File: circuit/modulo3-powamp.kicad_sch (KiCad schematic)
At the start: 60 parts, among them J1 HOLE, J2 HOLE, J3 HOLE, J4 HOLE, J5 CONN_01X04, Q1 BS170, SW1 reset, SW3 HEAD/AD, U2 TPA3220, U5 PWR_CONN, U6 AMPCTRL

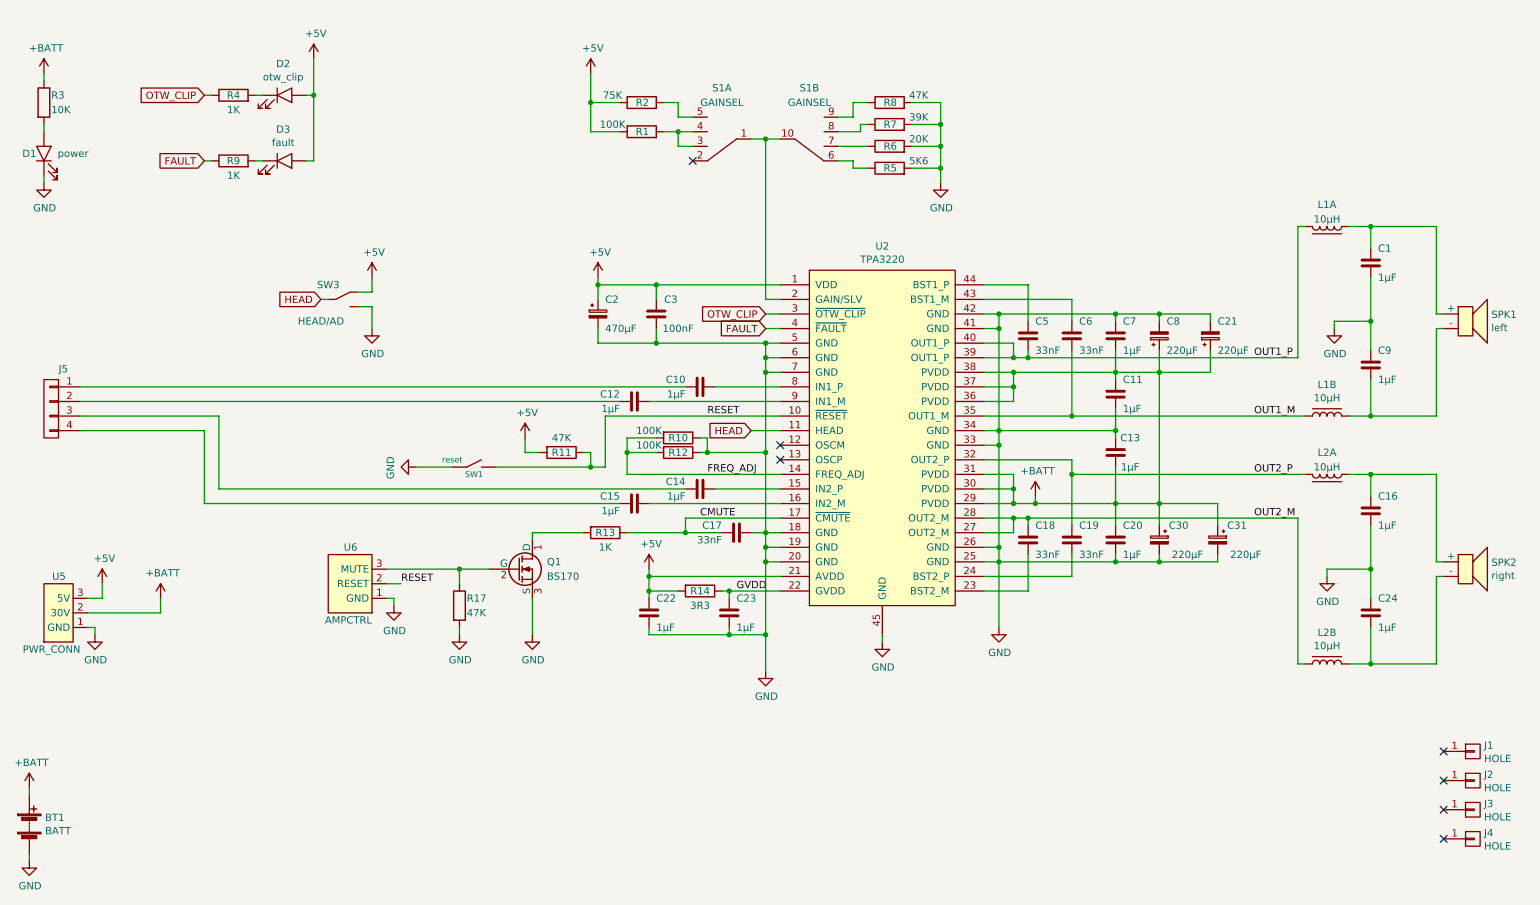
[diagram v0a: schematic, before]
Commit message: added ampctrl and diffaudio; started changing powamp
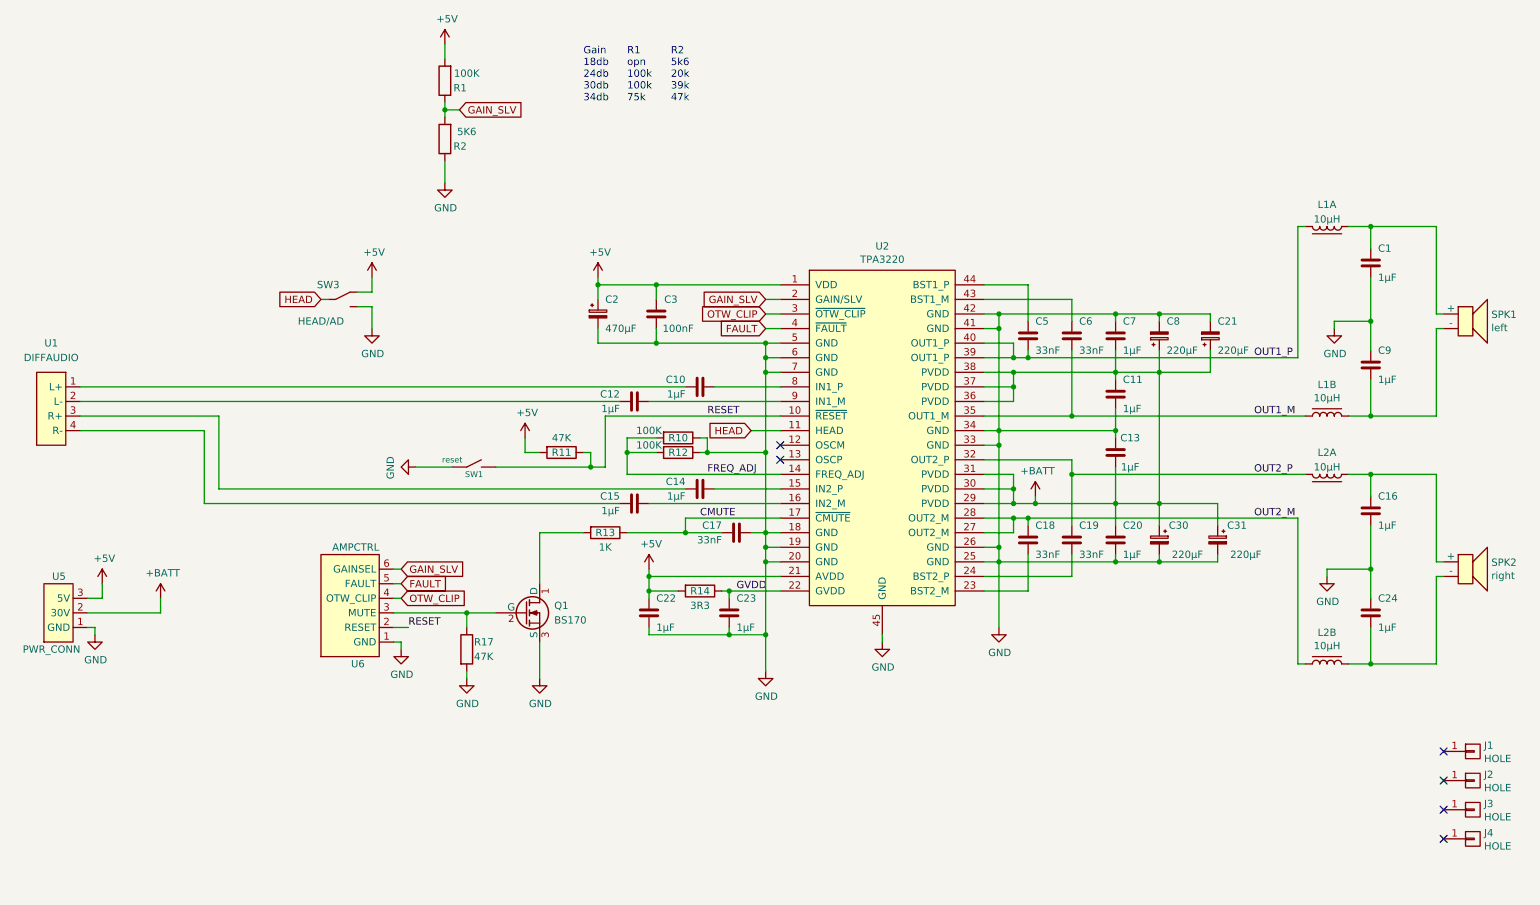
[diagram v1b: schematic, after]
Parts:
- removed BT1: BATT, myAmp:BATTERY, symbol myAmp:Battery
- removed D1: power, myAmp:LED_D3.0mm_PCBedge, symbol myAmp:LED
- removed D2: otw_clip, myAmp:LED_D3.0mm_PCBedge, symbol myAmp:LED
- removed D3: fault, myAmp:LED_D3.0mm_PCBedge, symbol myAmp:LED
- removed J5: CONN_01X04, myAmp:PIN_1x04, symbol myAmp:CONN_01X04
- removed R3: 10K, myAmp:R_0805, symbol myAmp:R
- removed R4, R9: 1K, myAmp:R_0805, symbol myAmp:R
- removed R5: 5K6, myAmp:R_0805, symbol myAmp:R
- removed R6: 20K, myAmp:R_0805, symbol myAmp:R
- removed R7: 39K, myAmp:R_0805, symbol myAmp:R
- removed R8: 47K, myAmp:R_0805, symbol myAmp:R
- removed S1: GAINSEL, myAmp:SR10010F-0204, symbol myAmp:SW_2P4T
- added U1: DIFFAUDIO, myAmp:DIFFAUDIO, symbol myAmp:DIFFAUDIO
- R1: footprint myAmp:R_0805 -> myAmp:R_10MM
- R2: value 75K -> 5K6; footprint myAmp:R_0805 -> myAmp:R_10MM
- U6: footprint myAmp:PIN_1x03 -> myAmp:AMPCTRL
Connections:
- net +5V: now also R1.2; no longer R1.1, R2.1
- net FAULT: now also U6.5 (FAULT)
- net GND: now also R2.1
- net OTW_CLIP: now also U6.4 (OTW_CLIP)
- net GAIN_SLV: now reaches U2.2 (GAIN/SLV)
- net GAIN_SLV: now also R1.1, R2.2, U6.6 (GAINSEL)
- net at C14.1: now also U1.3 (R+)
- net at C15.1: now also U1.4 (R-)
- net at C10.1: now also U1.1 (L+)
- net at C12.1: now also U1.2 (L-)
- no-connect marks 7 -> 6
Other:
- note added: "Gain 18db 24db 30db 34db"
- note added: "R1 opn 100k 100k 75k"
- note added: "R2 5k6 20k 39k 47k"
- moved on the sheet: Q1, R1, R17, R2

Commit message: got the pcs and holes sizes for mcu, poweamp and fv1
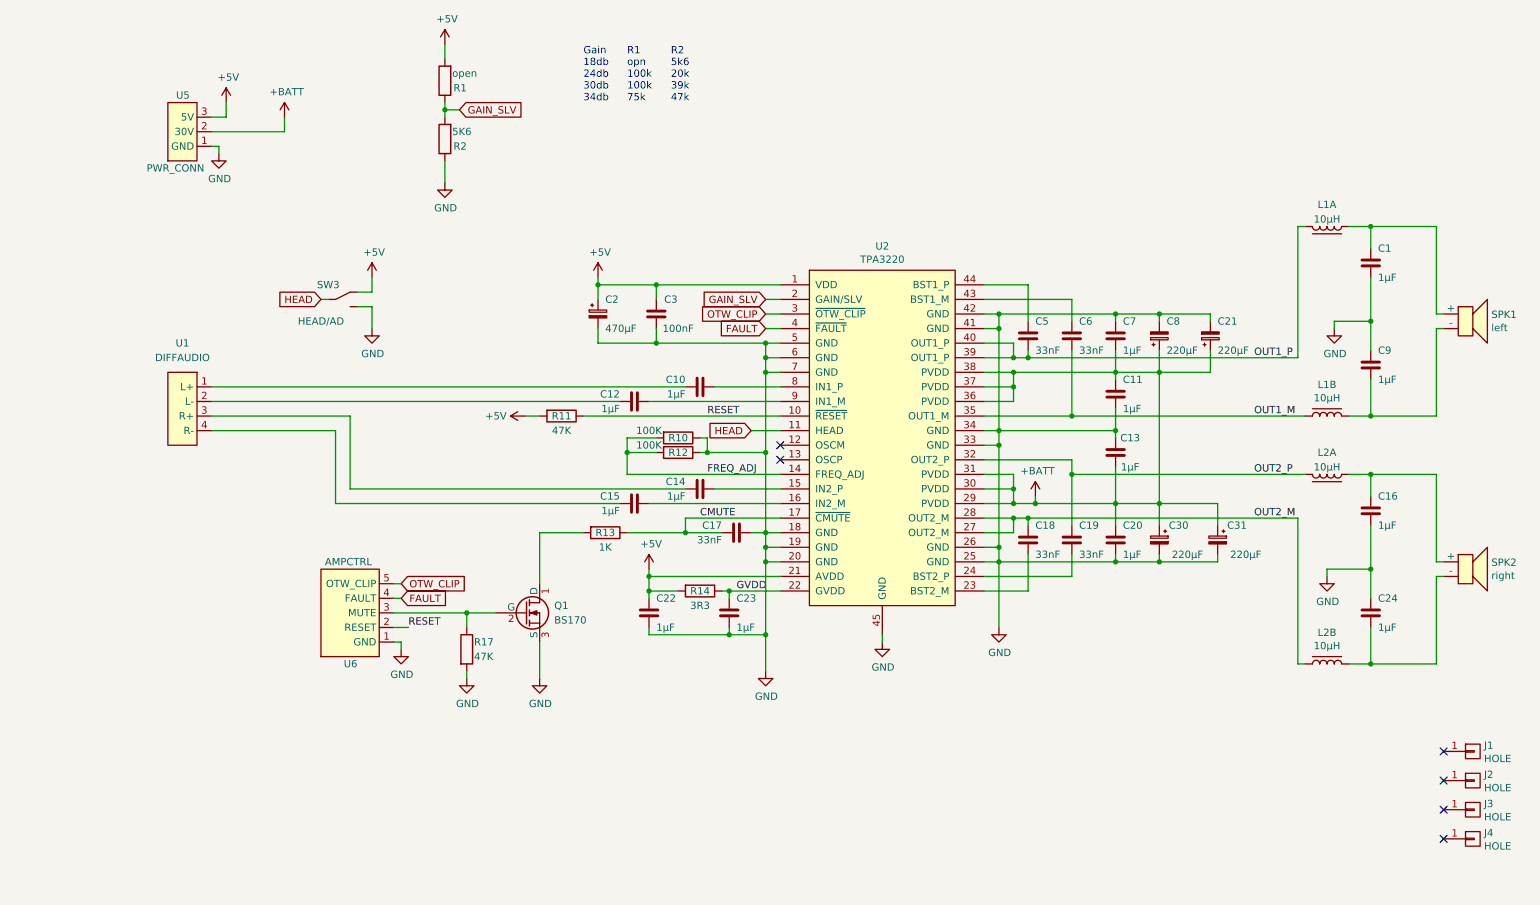
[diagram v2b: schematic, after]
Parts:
- removed SW1: reset, myAmp:Switch_2.5mm, symbol myAmp:SW_SIMPLE
- R1: value 100K -> open
- R10, R11, R12, R13: footprint myAmp:R_0805 -> myAmp:R_10MM
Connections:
- net FAULT: now also U6.4 (FAULT); no longer U6.5 (FAULT)
- net GAIN_SLV: no longer U6.6 (GAINSEL)
- net OTW_CLIP: now also U6.5 (OTW_CLIP); no longer U6.4 (OTW_CLIP)
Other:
- moved on the sheet: R11, U1, U5

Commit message: lotsa things :)
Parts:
- removed Q1: BS170, myAmp:TO-92_Inline_Wide, symbol myAmp:NMOS
- removed R17: 47K, myAmp:R_0805, symbol myAmp:R
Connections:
- net MUTE: now reaches R13.2
- net MUTE: now also U6.3 (MUTE)
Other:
- note added: "R1 open 100k 100k 75k"
- note removed: "R1 opn 100k 100k 75k"
- moved on the sheet: U6

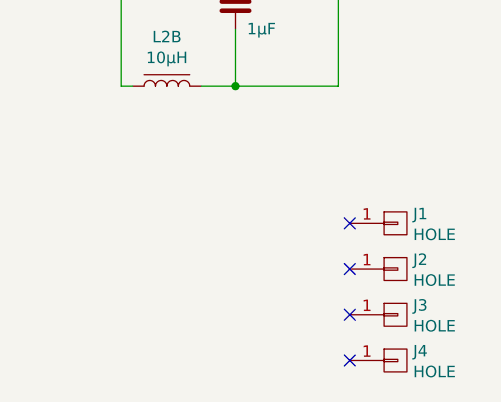
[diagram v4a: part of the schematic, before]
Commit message: tweaked power amp and fv1
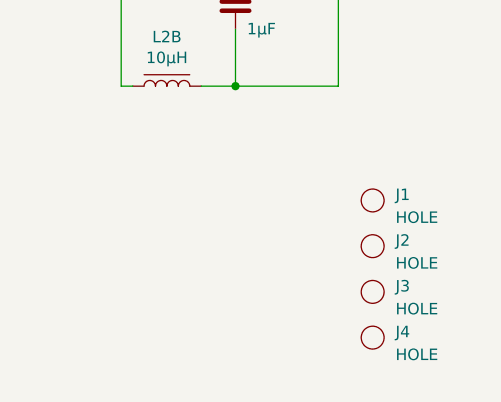
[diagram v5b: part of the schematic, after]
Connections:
- no-connect marks 6 -> 2
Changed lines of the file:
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@@
   )
   (no_connect (at 153.67 93.98))
-  (no_connect (at 269.24 149.86))
-  (no_connect (at 269.24 144.78))
-  (no_connect (at 269.24 160.02))
-  (no_connect (at 269.24 154.94))
   (no_connect (at 153.67 91.44))
   (wire (pts (xy 151.13 124.46) (xy 151.13 130.81))
@@
     (property "Intersheetrefs" "${INTERSHEET_REFS}" (at 228.6 154.94 0)
       (effects (font (size 1.27 1.27)) hide)
-    )
-  )
-  (symbol (lib_id "myAmp:HOLE") (at 274.32 144.78 0) (unit 1)
-    (in_bom yes) (on_board yes) (dnp no)
-    (property "Reference" "J1" (at 276.2758 143.7386 0)
-      (effects (font (size 1.27 1.27)) (justify left))
-    )
-    (property "Value" "HOLE" (at 276.2758 146.05 0)
-      (effects (font (size 1.27 1.27)) (justify left))
-    )
-    (property "Footprint" "myAmp:MountingHole" (at 274.32 144.78 0)
-      (effects (font (size 1.27 1.27)) hide)
-    )
-    (property "Datasheet" "" (at 274.32 144.78 0)
-      (effects (font (size 1.27 1.27)) hide)
-    )
-    (pin "1")
-    (instances
-      (project "modulo3-powamp"
-        (path "/e63e39d7-6ac0-4ffd-8aa3-1841a4541b55"
-          (reference "J1") (unit 1)
-        )
-      )
     )
   )
@@
     )
   )
-  (symbol (lib_id "myAmp:HOLE") (at 274.32 149.86 0) (unit 1)
-    (in_bom yes) (on_board yes) (dnp no)
-    (property "Reference" "J2" (at 276.2758 148.8186 0)
-      (effects (font (size 1.27 1.27)) (justify left))
-    )
-    (property "Value" "HOLE" (at 276.2758 151.13 0)
-      (effects (font (size 1.27 1.27)) (justify left))
-    )
-    (property "Footprint" "myAmp:MountingHole" (at 274.32 149.86 0)
-      (effects (font (size 1.27 1.27)) hide)
-    )
-    (property "Datasheet" "" (at 274.32 149.86 0)
-      (effects (font (size 1.27 1.27)) hide)
-    )
-    (pin "1")
-    (instances
-      (project "modulo3-powamp"
-        (path "/e63e39d7-6ac0-4ffd-8aa3-1841a4541b55"
-          (reference "J2") (unit 1)
-        )
-      )
-    )
-  )
-  (symbol (lib_id "myAmp:HOLE") (at 274.32 154.94 0) (unit 1)
-    (in_bom yes) (on_board yes) (dnp no)
-    (property "Reference" "J3" (at 276.2758 153.8986 0)
-      (effects (font (size 1.27 1.27)) (justify left))
-    )
-    (property "Value" "HOLE" (at 276.2758 156.21 0)
-      (effects (font (size 1.27 1.27)) (justify left))
-    )
-    (property "Footprint" "myAmp:MountingHole" (at 274.32 154.94 0)
-      (effects (font (size 1.27 1.27)) hide)
-    )
-    (property "Datasheet" "" (at 274.32 154.94 0)
-      (effects (font (size 1.27 1.27)) hide)
-    )
-    (pin "1")
-    (instances
-      (project "modulo3-powamp"
-        (path "/e63e39d7-6ac0-4ffd-8aa3-1841a4541b55"
-          (reference "J3") (unit 1)
-        )
-      )
-    )
-  )
-  (symbol (lib_id "myAmp:HOLE") (at 274.32 160.02 0) (unit 1)
-    (in_bom yes) (on_board yes) (dnp no)
-    (property "Reference" "J4" (at 276.2758 158.9786 0)
-      (effects (font (size 1.27 1.27)) (justify left))
-    )
-    (property "Value" "HOLE" (at 276.2758 161.29 0)
-      (effects (font (size 1.27 1.27)) (justify left))
-    )
-    (property "Footprint" "myAmp:MountingHole" (at 274.32 160.02 0)
-      (effects (font (size 1.27 1.27)) hide)
-    )
-    (property "Datasheet" "" (at 274.32 160.02 0)
-      (effects (font (size 1.27 1.27)) hide)
-    )
-    (pin "1")
-    (instances
-      (project "modulo3-powamp"
-        (path "/e63e39d7-6ac0-4ffd-8aa3-1841a4541b55"
-          (reference "J4") (unit 1)
-        )
-      )
-    )
-  )
   (symbol (lib_id "power:GND") (at 95.25 45.72 0) (unit 1)
     (in_bom yes) (on_board yes) (dnp no)
@@
     )
   )
+  (symbol (lib_name "HOLE_1") (lib_id "myAmp:HOLE") (at 271.78 147.32 0) (unit 1)
+    (in_bom yes) (on_board yes) (dnp no) (fields_autoplaced)
+    (property "Reference" "J2" (at 274.32 146.685 0)
+      (effects (font (size 1.27 1.27)) (justify left))
+    )
+    (property "Value" "HOLE" (at 274.32 149.225 0)
+      (effects (font (size 1.27 1.27)) (justify left))
+    )
+    (property "Footprint" "myAmp:MountingHole" (at 271.78 147.32 0)
+      (effects (font (size 1.27 1.27)) hide)
+    )
+    (property "Datasheet" "" (at 271.78 147.32 0)
+      (effects (font (size 1.27 1.27)) hide)
+    )
+    (instances
+      (project "modulo3-powamp"
+        (path "/e63e39d7-6ac0-4ffd-8aa3-1841a4541b55"
+          (reference "J2") (unit 1)
+        )
+      )
+    )
+  )
   (symbol (lib_id "power:+5V") (at 95.25 21.59 0) (unit 1)
     (in_bom yes) (on_board yes) (dnp no)
@@
     )
   )
+  (symbol (lib_name "HOLE_1") (lib_id "myAmp:HOLE") (at 271.78 142.24 0) (unit 1)
+    (in_bom yes) (on_board yes) (dnp no) (fields_autoplaced)
+    (property "Reference" "J1" (at 274.32 141.605 0)
+      (effects (font (size 1.27 1.27)) (justify left))
+    )
+    (property "Value" "HOLE" (at 274.32 144.145 0)
+      (effects (font (size 1.27 1.27)) (justify left))
+    )
+    (property "Footprint" "myAmp:MountingHole" (at 271.78 142.24 0)
+      (effects (font (size 1.27 1.27)) hide)
+    )
+    (property "Datasheet" "" (at 271.78 142.24 0)
+      (effects (font (size 1.27 1.27)) hide)
+    )
+    (instances
+      (project "modulo3-powamp"
+        (path "/e63e39d7-6ac0-4ffd-8aa3-1841a4541b55"
+          (reference "J1") (unit 1)
+        )
+      )
+    )
+  )
+  (symbol (lib_name "HOLE_1") (lib_id "myAmp:HOLE") (at 271.78 157.48 0) (unit 1)
+    (in_bom yes) (on_board yes) (dnp no) (fields_autoplaced)
+    (property "Reference" "J4" (at 274.32 156.845 0)
+      (effects (font (size 1.27 1.27)) (justify left))
+    )
+    (property "Value" "HOLE" (at 274.32 159.385 0)
+      (effects (font (size 1.27 1.27)) (justify left))
+    )
+    (property "Footprint" "myAmp:MountingHole" (at 271.78 157.48 0)
+      (effects (font (size 1.27 1.27)) hide)
+    )
+    (property "Datasheet" "" (at 271.78 157.48 0)
+      (effects (font (size 1.27 1.27)) hide)
+    )
+    (instances
+      (project "modulo3-powamp"
+        (path "/e63e39d7-6ac0-4ffd-8aa3-1841a4541b55"
+          (reference "J4") (unit 1)
+        )
+      )
+    )
+  )
   (symbol (lib_id "power:+5V") (at 109.22 86.36 90) (unit 1)
     (in_bom yes) (on_board yes) (dnp no)
@@
         )
       )
+    )
+  )
+  (symbol (lib_name "HOLE_1") (lib_id "myAmp:HOLE") (at 271.78 152.4 0) (unit 1)
+    (in_bom yes) (on_board yes) (dnp no) (fields_autoplaced)
+    (property "Reference" "J3" (at 274.32 151.765 0)
+      (effects (font (size 1.27 1.27)) (justify left))
+    )
+    (property "Value" "HOLE" (at 274.32 154.305 0)
+      (effects (font (size 1.27 1.27)) (justify left))
+    )
+    (property "Footprint" "myAmp:MountingHole" (at 271.78 152.4 0)
+      (effects (font (size 1.27 1.27)) hide)
+    )
+    (property "Datasheet" "" (at 271.78 152.4 0)
+      (effects (font (size 1.27 1.27)) hide)
+    )
+    (instances
+      (project "modulo3-powamp"
+        (path "/e63e39d7-6ac0-4ffd-8aa3-1841a4541b55"
+          (reference "J3") (unit 1)
+        )
+      )
